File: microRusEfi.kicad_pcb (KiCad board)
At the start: 2 copper layers, 80.6 x 93.7 mm, 240 parts, among them CN14 10nF, CN17 10nF, CN5 10nF, CN6 10nF, J1 USB_B_Micro, J2 Conn_02x05_Odd_Even, J3 Conn_01x02, J4 Conn_02x05_Counter_Clockwise, Q1 IPD30N06S2L-23, SW1 SW_Push, SW2 SW_Push, U1 STM32F407VGT6, U11 IS25LP256D-xM, U2 TLE8888QK, U3 Molex_48_pin, U31 MIC4427, U32 MIC4427, U33 MIC4427, U35 MCP6004, U36 MCP6004, U4 TLE9201SG, U46 MCP6004, U5 LM1117-3.3, U6 W25QxxJVS, U7 XC6206 3.3V, U8 MCP6004, X1 8MHz 20pF, Y2 32768 Hz

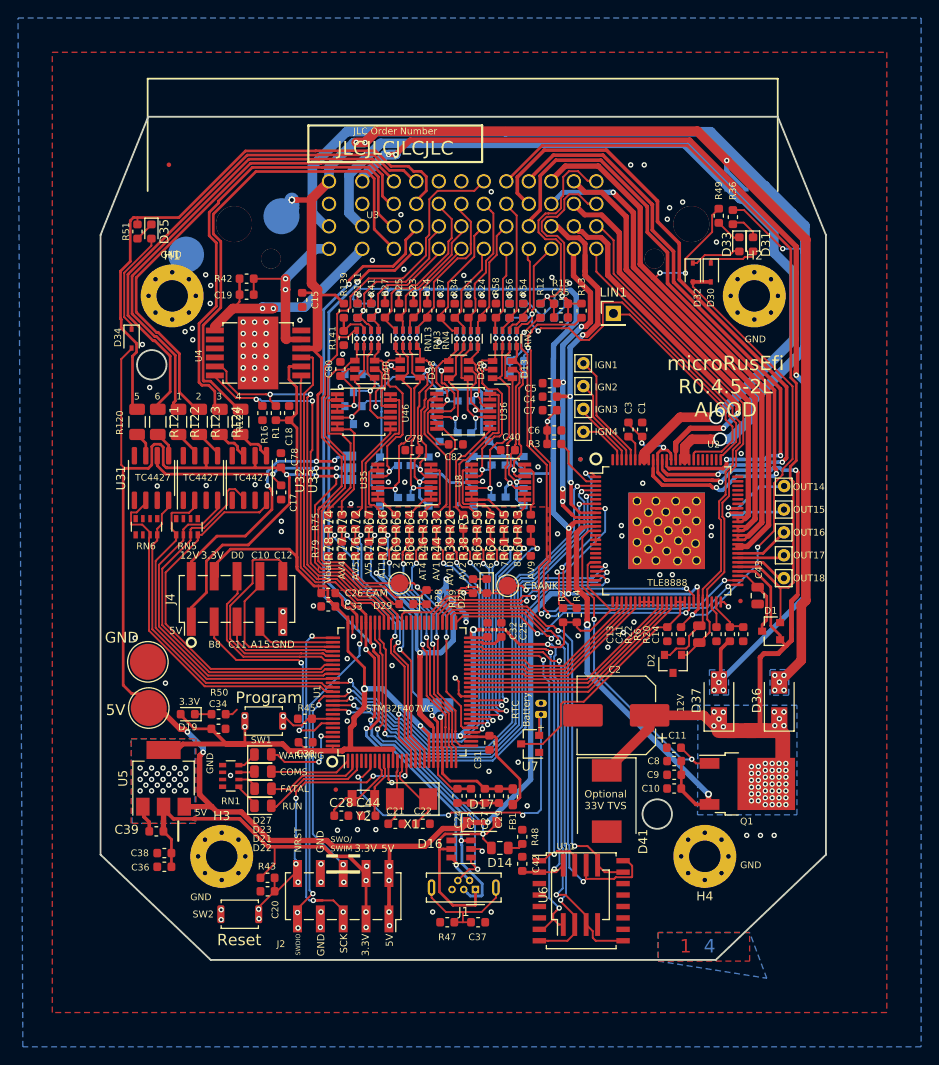
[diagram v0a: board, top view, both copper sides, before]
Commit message: Add diode and pull up on linbus. Fix some KiCAD 4.0 footprint problems
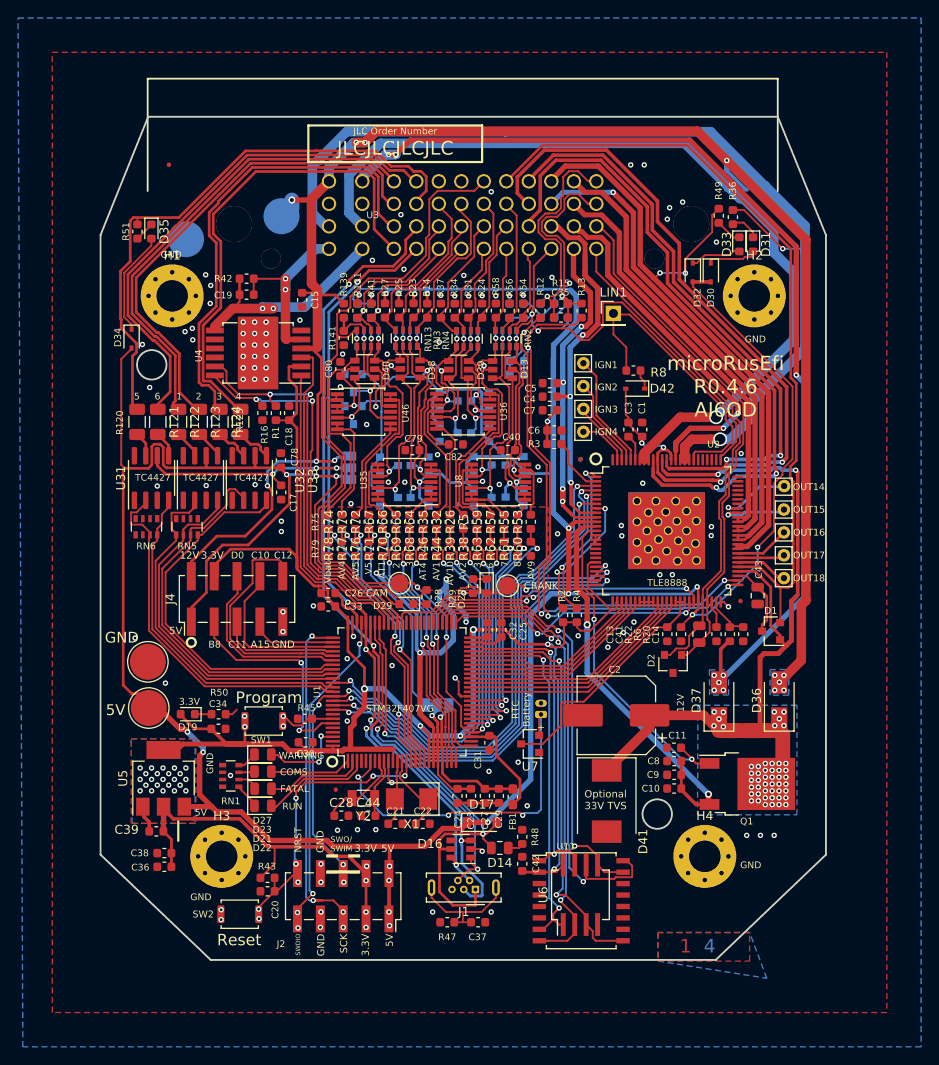
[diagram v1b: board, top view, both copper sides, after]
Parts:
- added D42: 1N4148WS, Diode_SMD:D_SOD-323, F.Cu at (80.0, 52.6)
- added R8: 1k, Resistor_SMD:R_0603_1608Metric, F.Cu at (79.8, 50.6)
- H1, H2, H3, H4: footprint Mounting_Holes:MountingHole_3.5mm_Pad_Via -> MountingHole:MountingHole_3.5mm_Pad_Via
- moved TP6 1.72 mm to (30.1, 36.0)
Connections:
- D30 pad 2: /5V -> Net-(D30-Pad2)
- D31 pad 2: Net-(D30-Pad1) -> Net-(D31-Pad2)
- R29 pad 1: Net-(D28-Pad1) -> Net-(R29-Pad1)
- R29 pad 2: GND -> Net-(R29-Pad2)
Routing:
- net /LINBUS: track 26.1 -> 33.1 mm
- net /12V_SAFE: track 100.9 -> 104.8 mm
- net Net-(D42-Pad1): track 0.00 -> 2.19 mm
- net Net-(R29-Pad2): track 0.00 -> 0.99 mm, vias 0 -> 1
- net GND: track 47.8 -> 46.8 mm, vias 118 -> 117
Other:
- board text added: "microRusEfi R0.4.6 AI6OD"
- board text removed: "microRusEfi R0.4.5-2L AI6OD"

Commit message: Move reset and boot buttons to be next to each other
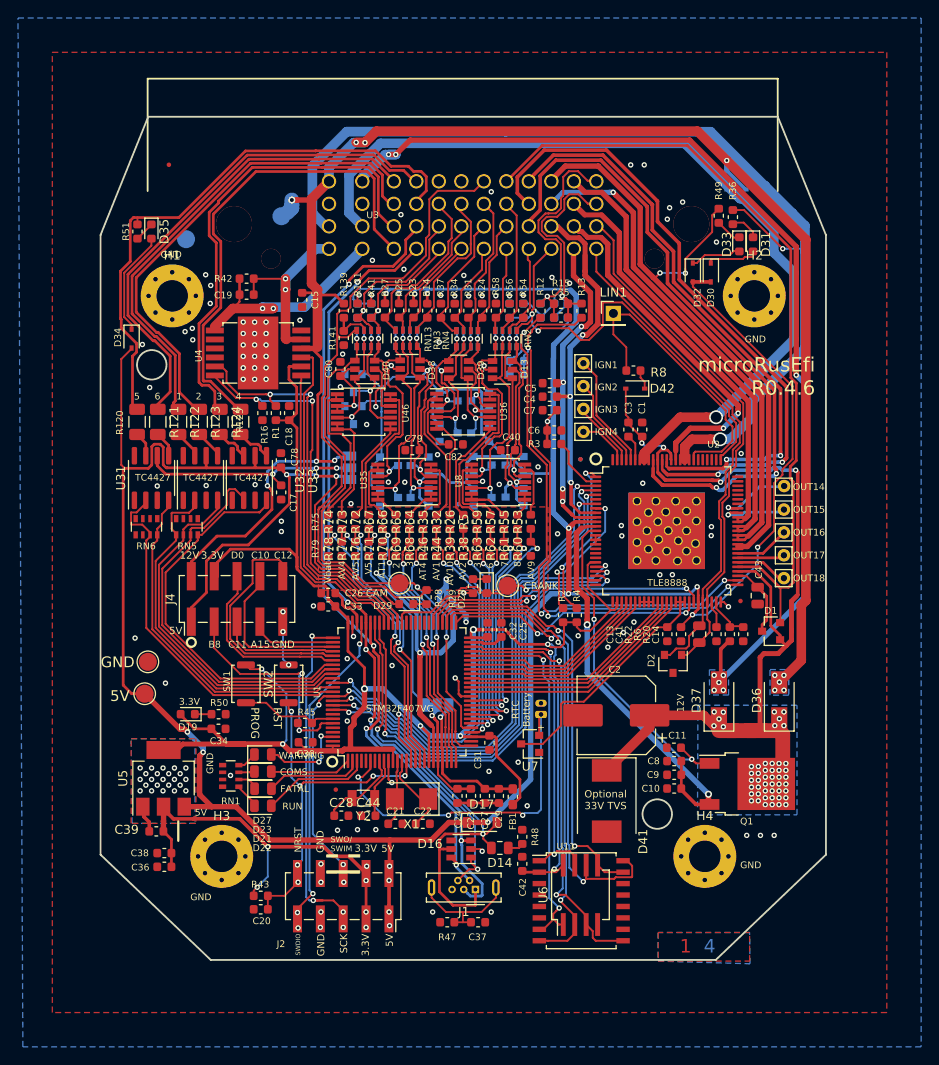
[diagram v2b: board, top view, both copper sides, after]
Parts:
- TP1, TP2, TP5, TP6: footprint TestPoint:TestPoint_Pad_D4.0mm -> TestPoint:TestPoint_Pad_D2.0mm
- moved LOGO1 77.6 mm to (123.2, 119.2)
- moved SW2 26.2 mm to (41.5, 85.4), turned to 90 degrees
- moved SW1 4.59 mm to (36.8, 85.4), turned to 270 degrees
- moved C20 2.14 mm to (38.4, 110.5)
- moved R43 2.14 mm to (38.4, 109.0)
- moved TP1 1.65 mm to (25.5, 86.5)
- moved R45 0.47 mm to (43.3, 89.8)
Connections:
- D16 pad 4: Net-(D16-Pad4) -> (no net)
- D28 pad 1: Net-(D28-Pad1) -> (no net)
- D30 pad 1: Net-(D30-Pad1) -> (no net)
- D30 pad 2: Net-(D30-Pad2) -> (no net)
- D31 pad 2: Net-(D31-Pad2) -> (no net)
- R29 pad 1: Net-(R29-Pad1) -> (no net)
- R29 pad 2: Net-(R29-Pad2) -> (no net)
- RN6 pad 5: Net-(RN6-Pad5) -> (no net)
- RN6 pad 6: Net-(RN6-Pad6) -> (no net)
- U1 pad 4: /MCU/PE5 -> (no net)
- U1 pad 5: /MCU/PE6 -> (no net)
- U1 pad 57: /MCU/PD10 -> (no net)
- U1 pad 58: /MCU/PD11 -> (no net)
- U1 pad 59: /MCU/PD12 -> (no net)
- U1 pad 60: /MCU/PD13 -> (no net)
- U1 pad 61: /MCU/PD14 -> (no net)
- U1 pad 62: /MCU/PD15 -> (no net)
- U1 pad 7: /MCU/PC13 -> (no net)
- U1 pad 93: /MCU/PB7 -> (no net)
- U1 pad 96: /MCU/PB9 -> (no net)
- U1 pad 97: /MCU/PE0 -> (no net)
- U11 pad 11: Net-(U11-Pad11) -> (no net)
- U11 pad 12: Net-(U11-Pad12) -> (no net)
- U11 pad 13: Net-(U11-Pad13) -> (no net)
- U11 pad 14: Net-(U11-Pad14) -> (no net)
- U11 pad 3: Net-(U11-Pad3) -> (no net)
- U11 pad 4: Net-(U11-Pad4) -> (no net)
- U11 pad 5: Net-(U11-Pad5) -> (no net)
- U11 pad 6: Net-(U11-Pad6) -> (no net)
- U2 pad 17: /TLE8888-1QK/OUT_20 -> (no net)
- U2 pad 18: /TLE8888-1QK/OUT_19 -> (no net)
- U2 pad 69: /TLE8888-1QK/DFB8 -> (no net)
- U2 pad 70: /TLE8888-1QK/DFB9 -> (no net)
- U2 pad 71: /TLE8888-1QK/OUT_8 -> (no net)
- U2 pad 72: /TLE8888-1QK/OUT_9 -> (no net)
- U2 pad 73: /TLE8888-1QK/DFB10 -> (no net)
- U2 pad 74: /TLE8888-1QK/OUT_10 -> (no net)
- U2 pad 76: Net-(U2-Pad76) -> (no net)
- U2 pad 77: Net-(U2-Pad77) -> (no net)
- U2 pad 78: Net-(U2-Pad78) -> (no net)
- U2 pad 79: Net-(U2-Pad79) -> (no net)
- U2 pad 80: Net-(U2-Pad80) -> (no net)
- U2 pad 81: Net-(U2-Pad81) -> (no net)
- U31 pad 1: Net-(U31-Pad1) -> (no net)
- U31 pad 8: Net-(U31-Pad8) -> (no net)
- U32 pad 1: Net-(U32-Pad1) -> (no net)
- U32 pad 8: Net-(U32-Pad8) -> (no net)
- U33 pad 1: Net-(U33-Pad1) -> (no net)
- U33 pad 8: Net-(U33-Pad8) -> (no net)
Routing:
- net /VDD: track 260.4 -> 271.3 mm, vias 35 -> 37
- net (no net): track 0.00 -> 9.36 mm, vias 0 -> 1
- net /MCU/NRST: track 33.3 -> 39.5 mm, vias 7 -> 6
- net Net-(D30-Pad1): track 5.82 -> 0.00 mm
- net /MCU/BOOT0: track 6.41 -> 10.8 mm, vias 2 -> 0
- net GND: track 46.8 -> 49.4 mm, vias 117 -> 116
- net Net-(D28-Pad1): track 1.52 -> 0.00 mm
- net Net-(R29-Pad2): track 0.99 -> 0.00 mm, vias 1 -> 0
- net /hi-lo/Ign1_MCU: track 39.8 -> 40.7 mm
- net /hi-lo/Ign4_MCU: track 41.3 -> 42.2 mm
- net /hi-lo/Ign3_MCU: track 43.0 -> 43.9 mm
- net /hi-lo/Ign2_MCU: track 39.3 -> 40.2 mm
- net /MCU/PD14: track 0.71 -> 0.00 mm
- net /hi-lo/GP5_MCU: track 40.4 -> 40.9 mm
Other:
- board text added: "PROG"
- board text added: "RST"
- board text added: "microRusEfi R0.4.6"
- board text removed: "JLC Order Number"
- board text removed: "JLCJLCJLCJLC"
- board text removed: "Program"
- board text removed: "Reset"
- board text removed: "microRusEfi R0.4.6 AI6OD"

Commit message: Fix a few DRC errors probably introduced by me
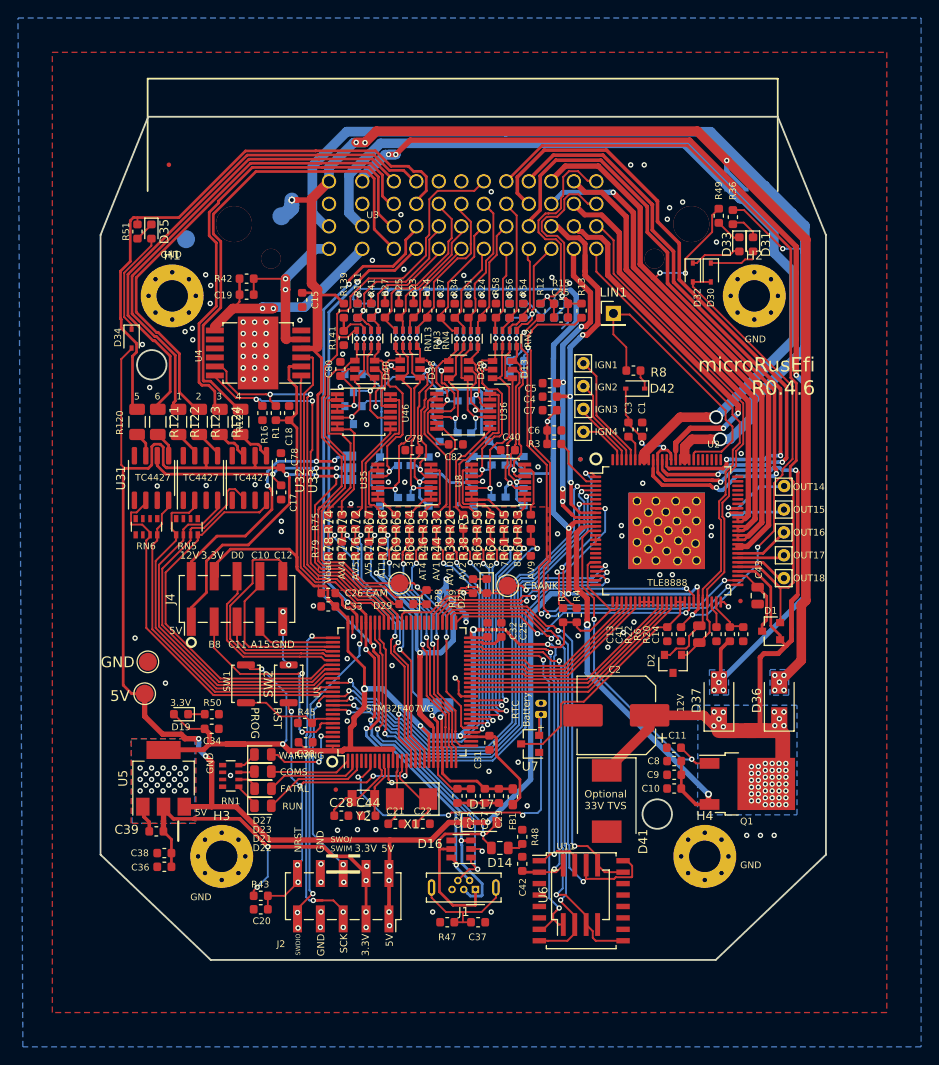
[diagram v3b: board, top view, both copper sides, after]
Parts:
- moved C34 0.75 mm to (33.0, 90.4)
- moved D19 0.75 mm to (29.5, 88.8)
- moved R50 0.75 mm to (33.0, 88.8)
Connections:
- D28 pad 1: (no net) -> Net-(D28-Pad1)
- D30 pad 1: (no net) -> Net-(D30-Pad1)
- D30 pad 2: (no net) -> /5V
- D31 pad 2: (no net) -> Net-(D30-Pad1)
- R29 pad 1: (no net) -> Net-(D28-Pad1)
- R29 pad 2: (no net) -> GND
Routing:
- net /AV9: track 52.5 -> 13.6 mm, vias 2 -> 1
- net (no net): track 9.36 -> 0.00 mm, vias 1 -> 0
- net Net-(D30-Pad1): track 0.00 -> 5.69 mm
- net Net-(D28-Pad1): track 0.00 -> 1.52 mm
- net /5V: track 495.2 -> 496.5 mm
- net GND: track 49.4 -> 50.4 mm, vias 116 -> 117
- net /VDD: track 271.3 -> 270.5 mm
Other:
- rule trace_min: 0.2032 -> 0

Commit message: Clean up tracks and vias
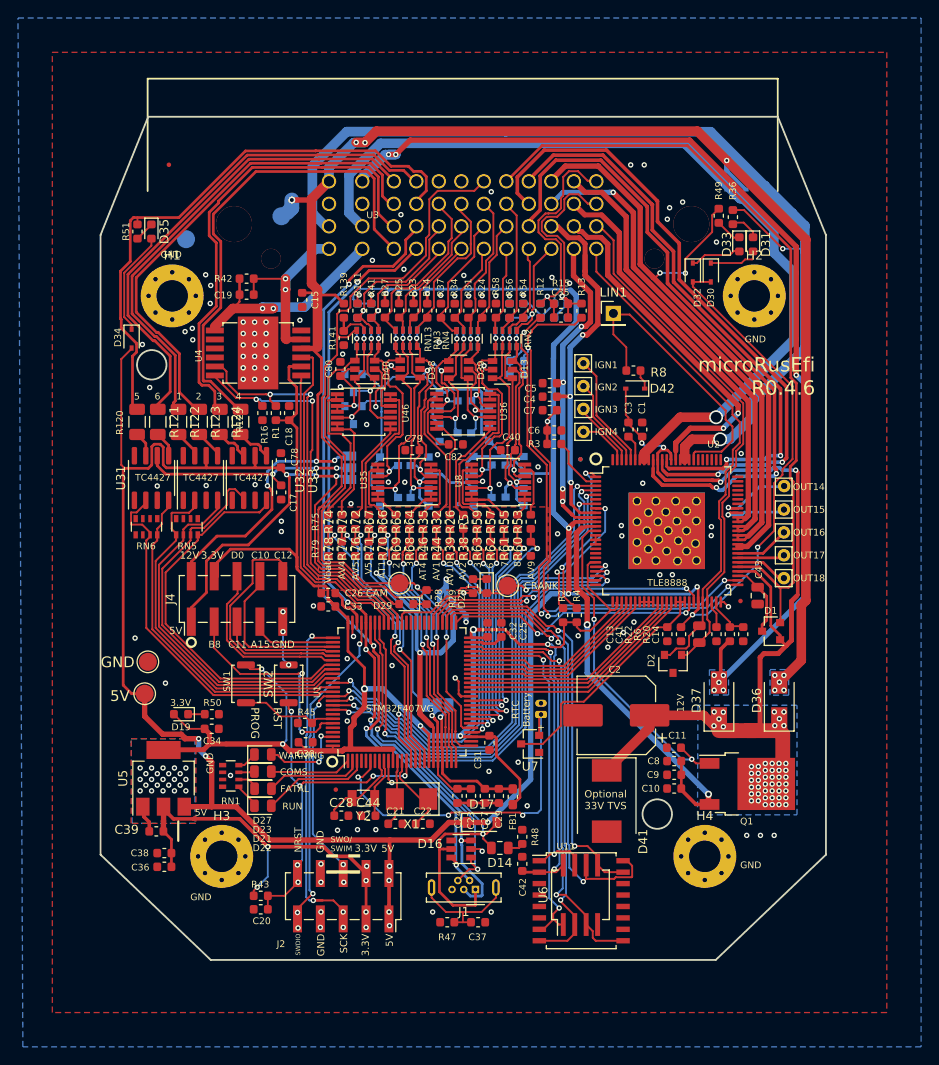
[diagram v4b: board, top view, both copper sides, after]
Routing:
- net /VDD: track 270.5 -> 268.8 mm
- net GND: track 50.4 -> 48.9 mm

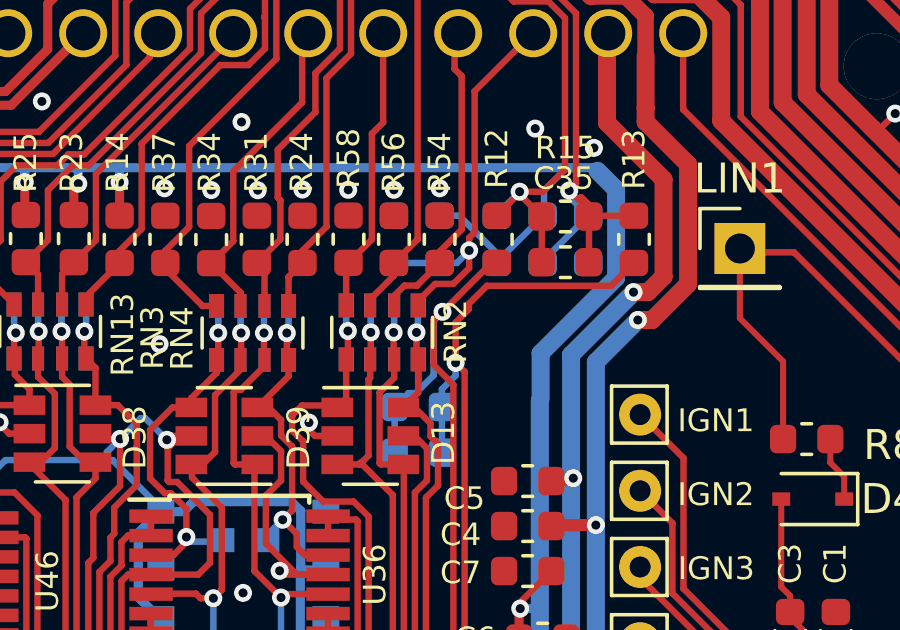
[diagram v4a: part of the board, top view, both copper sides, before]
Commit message: Missing GND connection on CRNK-
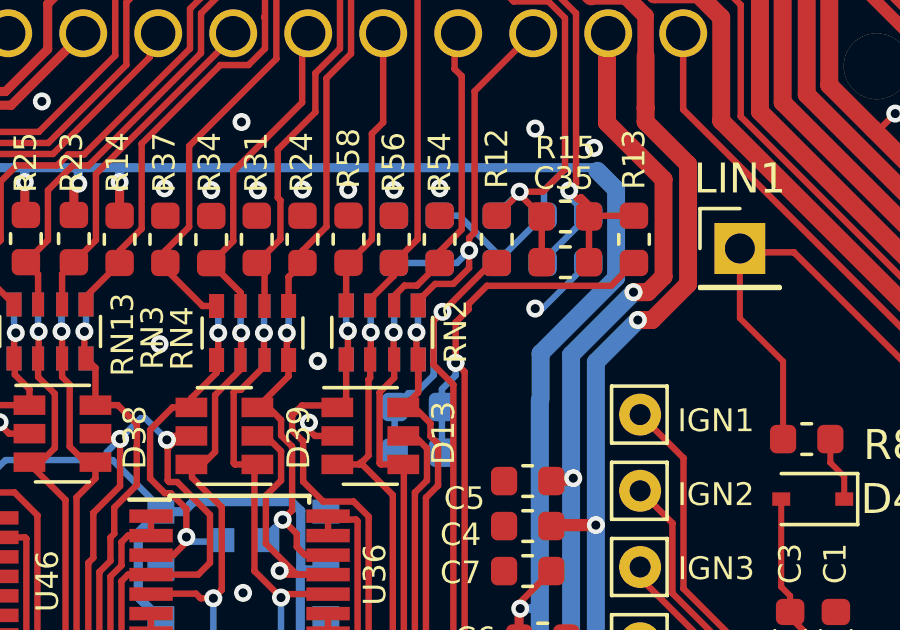
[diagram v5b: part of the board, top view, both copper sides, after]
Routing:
- net GND: track 48.9 -> 51.3 mm, vias 117 -> 119
